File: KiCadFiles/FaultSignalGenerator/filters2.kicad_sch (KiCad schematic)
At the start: 65 parts

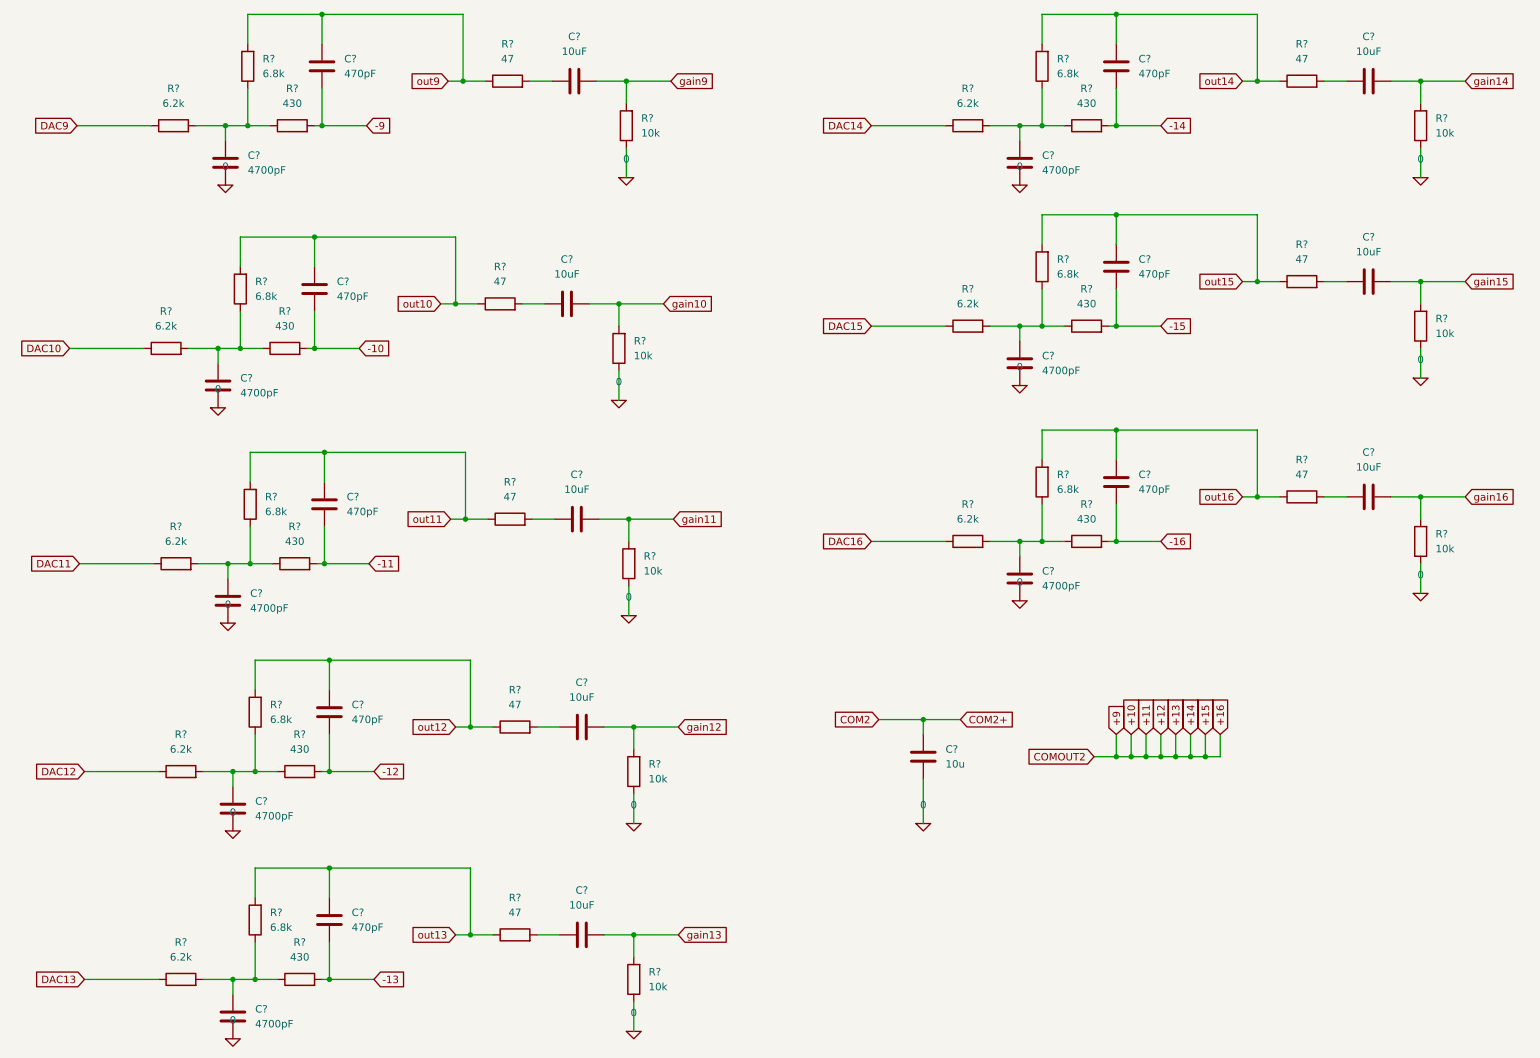
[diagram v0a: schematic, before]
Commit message: Finish schematic, start on PCB
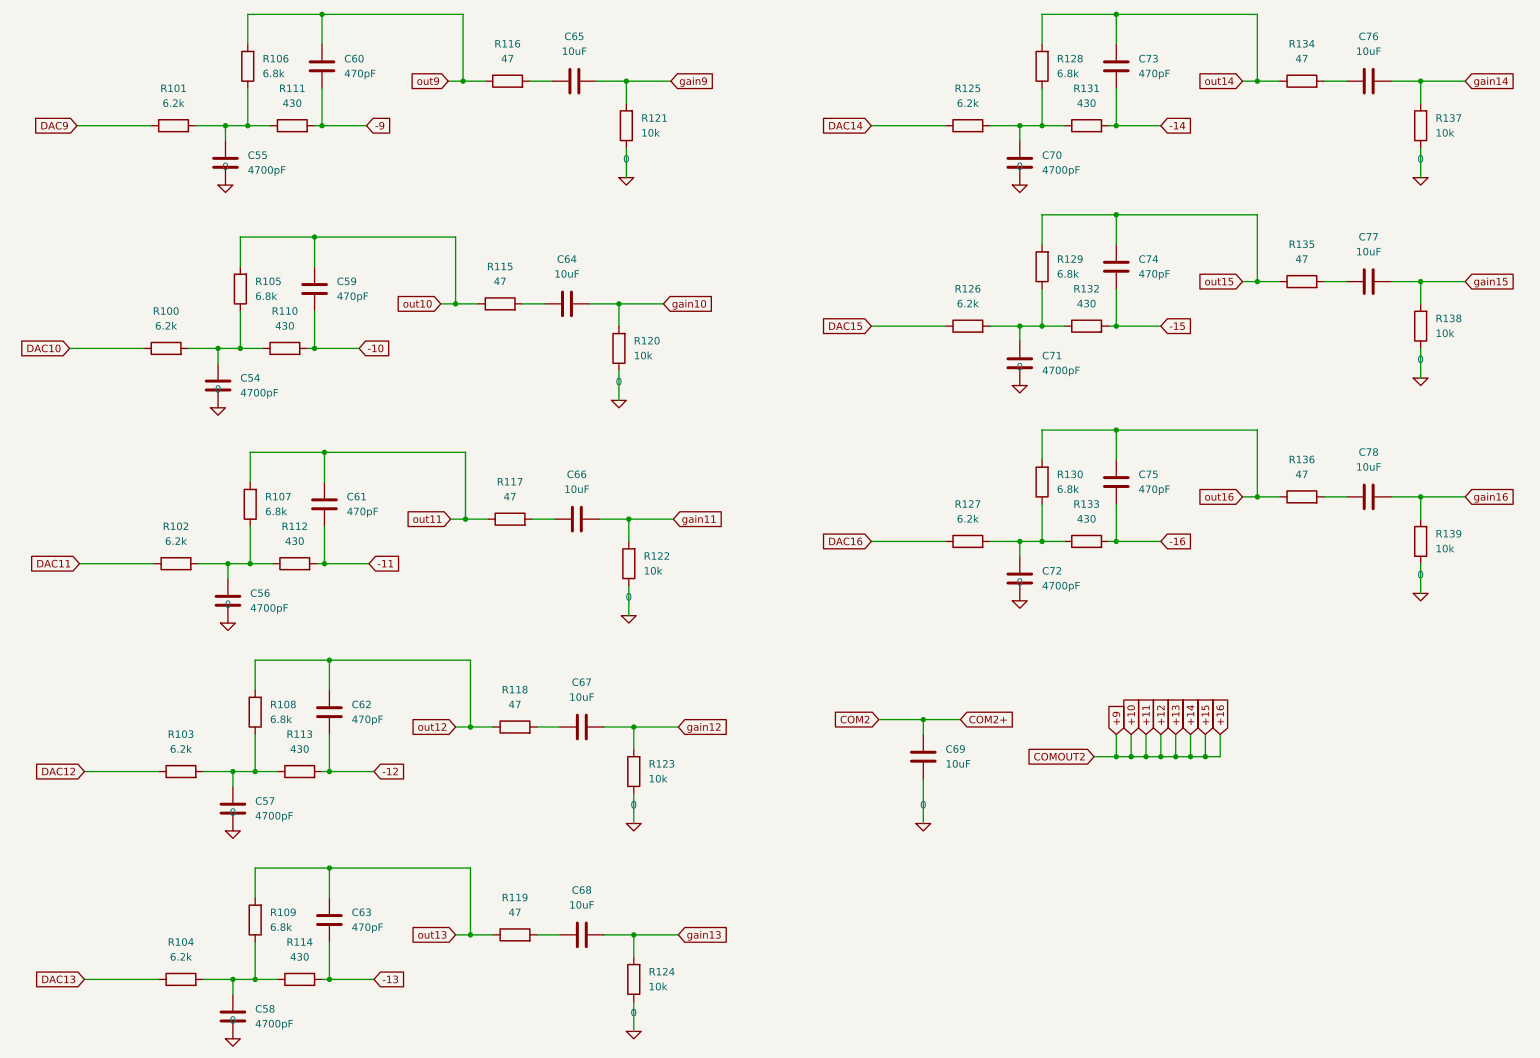
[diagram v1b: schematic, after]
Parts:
- C54, C55, C56, C57, C58, C70, C71, C72: renamed from C?; footprint Capacitor_SMD:C_1812_4532Metric_Pad1.57x3.40mm_HandSolder -> Capacitor_SMD:C_1206_3216Metric_Pad1.33x1.80mm_HandSolder; Spice_Model 4700p -> (none); Spice_Netlist_Enabled Y -> (none); Spice_Primitive C -> (none)
- C59, C60, C61, C62, C63, C73, C74, C75: renamed from C?; footprint Capacitor_SMD:C_1812_4532Metric_Pad1.57x3.40mm_HandSolder -> Capacitor_SMD:C_1206_3216Metric_Pad1.33x1.80mm_HandSolder; Spice_Model 470p -> (none); Spice_Netlist_Enabled Y -> (none); Spice_Primitive C -> (none)
- C64, C65, C66, C67, C68, C76, C77, C78: renamed from C?; footprint Capacitor_SMD:C_1812_4532Metric_Pad1.57x3.40mm_HandSolder -> Capacitor_SMD:C_1206_3216Metric_Pad1.33x1.80mm_HandSolder; Spice_Model 10u -> (none); Spice_Netlist_Enabled Y -> (none); Spice_Primitive C -> (none)
- C69: renamed from C?; value 10u -> 10uF; footprint Capacitor_SMD:C_1812_4532Metric_Pad1.57x3.40mm_HandSolder -> Capacitor_SMD:C_1206_3216Metric_Pad1.33x1.80mm_HandSolder; Spice_Model 10u -> (none); Spice_Netlist_Enabled Y -> (none); Spice_Primitive C -> (none)
- R100, R101, R102, R103, R104, R125, R126, R127: renamed from R?; footprint Resistor_SMD:R_0603_1608Metric_Pad0.98x0.95mm_HandSolder -> Resistor_SMD:R_1206_3216Metric; Spice_Model 6.2k -> (none); Spice_Netlist_Enabled Y -> (none); Spice_Primitive R -> (none)
- R105, R106, R107, R108, R109, R128, R129, R130: renamed from R?; footprint Resistor_SMD:R_0603_1608Metric_Pad0.98x0.95mm_HandSolder -> Resistor_SMD:R_1206_3216Metric; Spice_Model 6.8k -> (none); Spice_Netlist_Enabled Y -> (none); Spice_Primitive R -> (none)
- R110, R111, R112, R113, R114, R131, R132, R133: renamed from R?; footprint Resistor_SMD:R_0603_1608Metric_Pad0.98x0.95mm_HandSolder -> Resistor_SMD:R_1206_3216Metric; Spice_Model 430 -> (none); Spice_Netlist_Enabled Y -> (none); Spice_Primitive R -> (none)
- R115, R116, R117, R118, R119, R134, R135, R136: renamed from R?; footprint Resistor_SMD:R_0603_1608Metric_Pad0.98x0.95mm_HandSolder -> Resistor_SMD:R_1206_3216Metric; Spice_Model 47 -> (none); Spice_Netlist_Enabled Y -> (none); Spice_Primitive R -> (none)
- R120, R121, R122, R123, R124, R137, R138, R139: renamed from R?; footprint Resistor_SMD:R_0603_1608Metric_Pad0.98x0.95mm_HandSolder -> Resistor_SMD:R_1206_3216Metric
